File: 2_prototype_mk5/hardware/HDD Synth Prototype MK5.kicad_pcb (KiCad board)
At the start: 2 copper layers, 100.3 x 69.9 mm, 97 parts, among them J1 Micro_SD_Card, J2 Conn_01x03, J4 USB_C_Receptacle_USB2.0_16P, J6 Conn_01x04_Pin, J7 Conn_01x05, Q1 2N7002, U1 Optocoupler_DC_PhotoNPN_AKEC, U2 MAX98357A, U3 W25Q32JVSSIQ, U4 NCP1117-3.3_SOT223, U5 RP2350_60QFN, U6 TPS63020DSJR, Y1 ABM8-272-T3

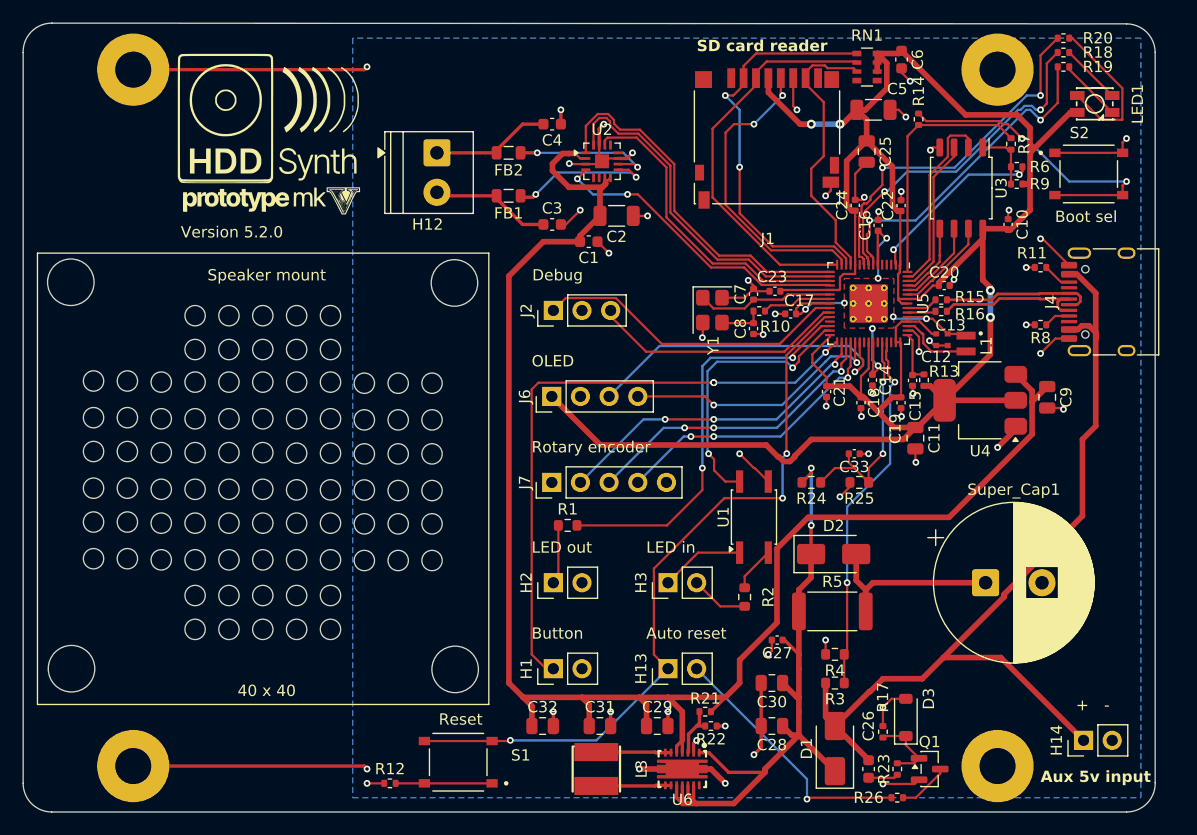
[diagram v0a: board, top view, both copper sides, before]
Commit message: Cost reductions for JCLPCB
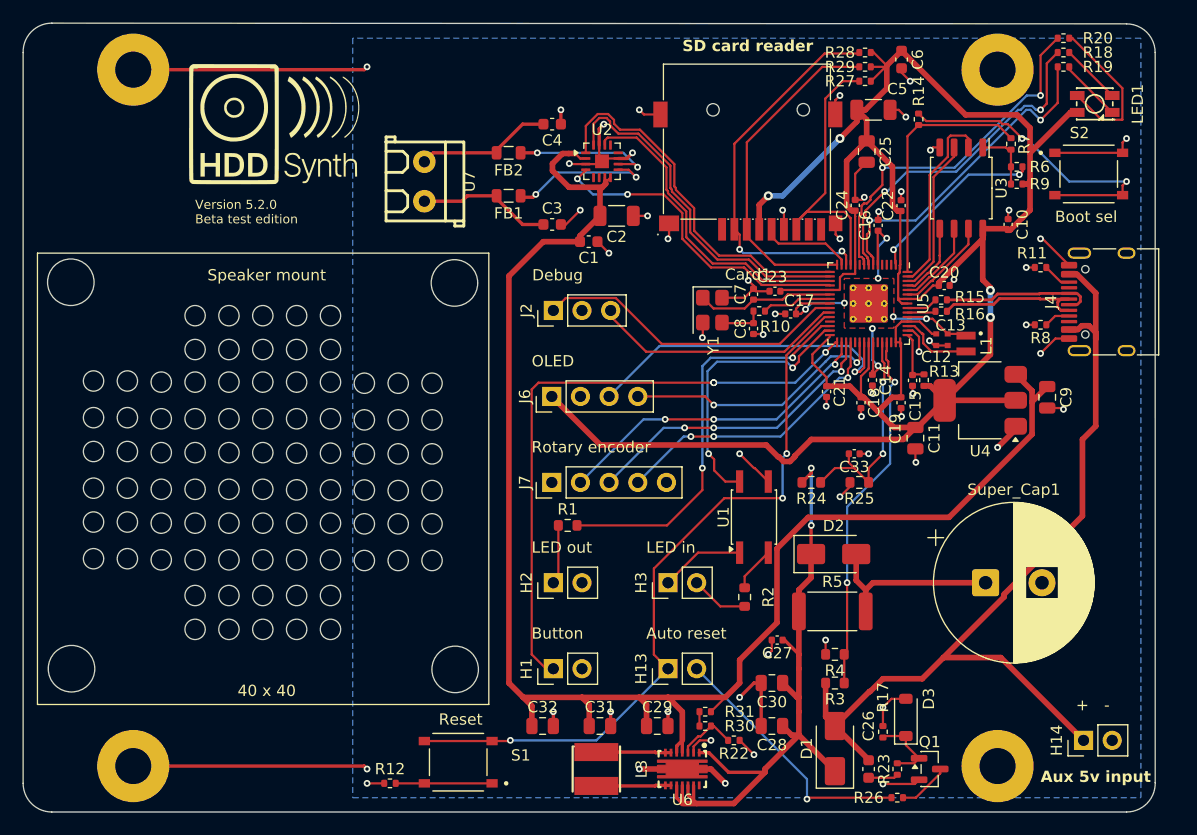
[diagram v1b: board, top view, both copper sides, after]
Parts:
- removed the G*** at (96.5, 57.1)
- removed H12: Conn_01x02, TerminalBlock_Phoenix:TerminalBlock_Phoenix_PT-1,5-2-3.5-H_1x02_P3.50mm_Horizontal
- removed J1: Micro_SD_Card, Connector_Card:microSD_HC_Hirose_DM3D-SF
- removed R21: 1.6M, Resistor_SMD:R_0402_1005Metric
- removed RN1: 47K, Resistor_SMD:R_Array_Convex_4x0603
- added Card1: TF-015, easyeda2kicad:TF-SMD_TF-015, F.Cu at (137.9, 60.1)
- added G***: LOGO, Custom:HDDSynth_Logo_18mm, F.Cu at (96.5, 55.9)
- added R27: 47K, Resistor_SMD:R_0402_1005Metric, F.Cu at (148.3, 52.1)
- added R28: 47K, Resistor_SMD:R_0402_1005Metric, F.Cu at (148.3, 49.5)
- added R29: 47K, Resistor_SMD:R_0402_1005Metric, F.Cu at (148.3, 50.8)
- added R30: 100K, Resistor_SMD:R_0402_1005Metric, F.Cu at (134.1, 109.2)
- added R31: 100K, Resistor_SMD:R_0402_1005Metric, F.Cu at (134.1, 108.0)
- added U7: KF350-3.5-2P, easyeda2kicad:CONN-TH_P3.50_KF350-3.5-2P, F.Cu at (109.2, 61.0)
- D2: value SS12 -> SS14
- R10, R12, R14: value 1k -> 1K
- R18: value 56R -> 33R
- R19: value 270R -> 200R
- R22: value 180K -> 22K
- moved R22 2.39 mm to (136.7, 110.5)
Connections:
- U5 pad 35: /RP2350/OLED_SDA -> /RP2350/GPIO23
- U5 pad 36: /RP2350/OLED_SCL -> /RP2350/OLED_SDA
- U5 pad 37: /RP2350/GPIO25 -> /RP2350/OLED_SCL
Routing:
- net /RP2350/SD_SCK: track 27.2 -> 8.15 mm, vias 2 -> 0
- net +3V3: track 204.8 -> 210.9 mm
- net GND: track 149.2 -> 155.2 mm, vias 54 -> 57
- net /RP2350/SD_MOSI: track 35.6 -> 30.1 mm
- net /RP2350/SD_CS: track 36.8 -> 34.4 mm
- net Net-(C4-Pad2): track 10.6 -> 12.1 mm
- net /RP2350/AMP_SDMODE: track 27.4 -> 28.7 mm
- net Net-(R30-Pad1): track 0.00 -> 1.27 mm
- net /RP2350/SD_MISO: track 24.6 -> 25.8 mm
- net Net-(C3-Pad1): track 10.8 -> 11.9 mm
- net Net-(U6-FB): track 4.81 -> 5.38 mm
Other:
- board text added: "Version 5.2.0 Beta test edition"
- board text removed: "Version 5.2.0"
